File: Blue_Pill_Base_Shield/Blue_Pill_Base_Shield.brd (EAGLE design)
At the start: 54.2 x 36.7 mm, 15 parts, among them J1 4P-2.0, J2 4P-2.0, J3 4P-2.0, J4 4P-2.0, J5 4P-2.0, J6 4P-2.0, J7 4P-2.0, J8 4P-2.0

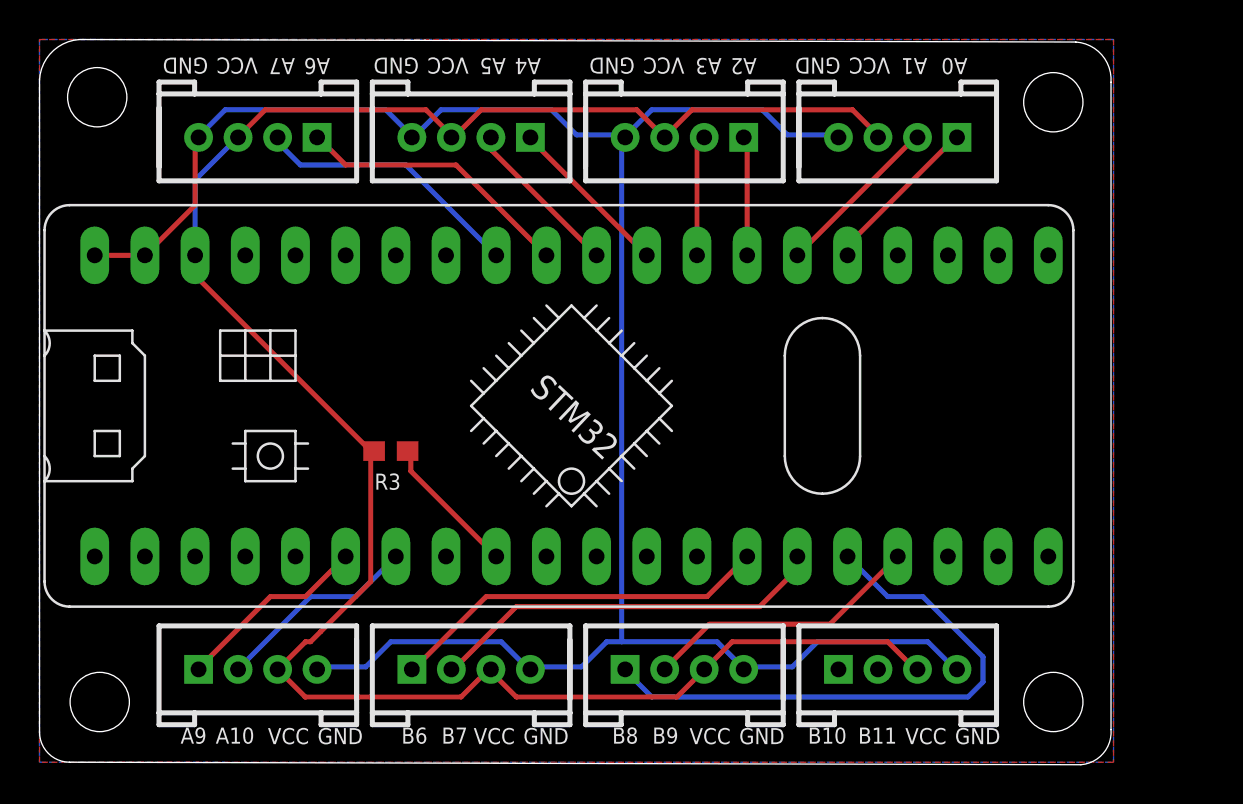
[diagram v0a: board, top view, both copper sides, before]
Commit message: Update Blue Pill Shield to add UART header
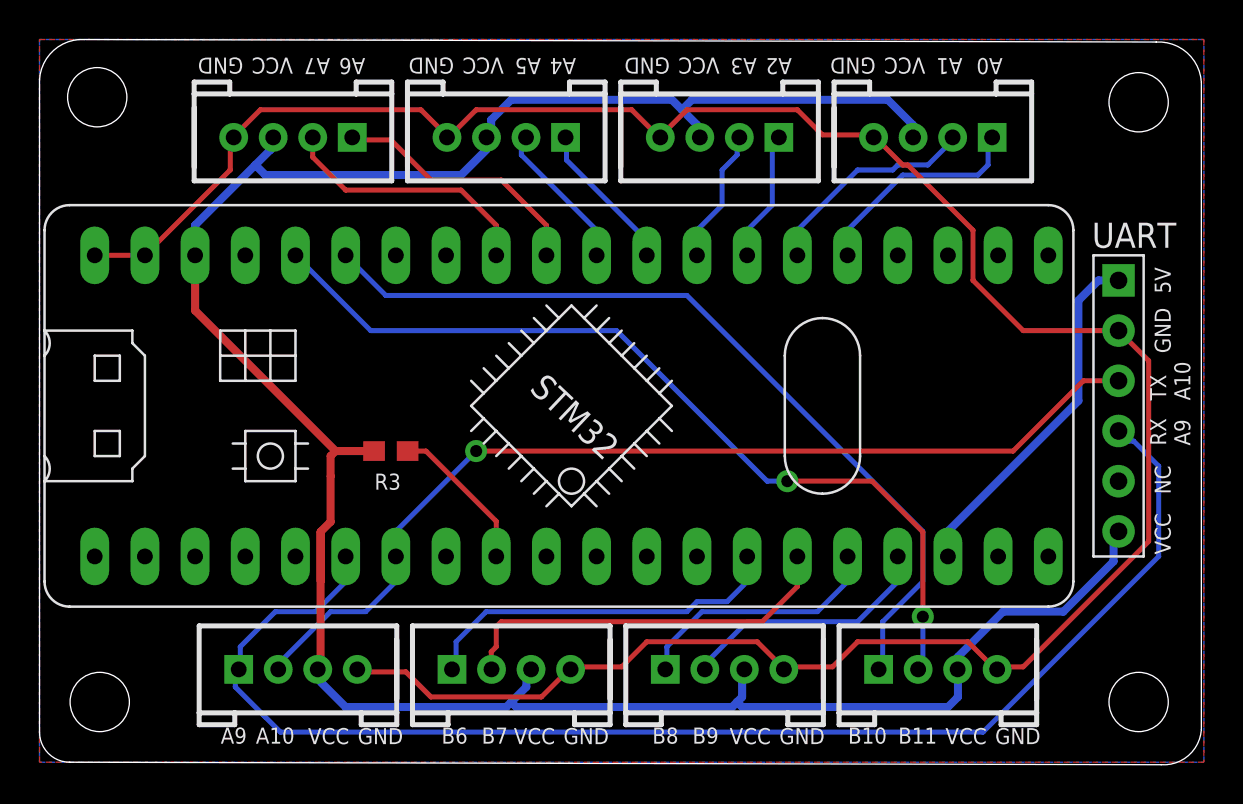
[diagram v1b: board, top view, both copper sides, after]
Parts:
- added UART: YELLOW-6P-2.54, Seeed-Connector:H6-2.54
- moved U$3 4.32 mm to (55.9, 32.9)
- moved U$4 4.32 mm to (55.9, 2.54)
- moved J1 2.03 mm to (13.3, 4.19)
- moved J2 2.03 mm to (24.1, 4.19)
- moved J3 2.03 mm to (34.9, 4.19)
- moved J4 2.03 mm to (45.7, 4.19)
- moved J6 1.78 mm to (23.9, 31.1)
- moved J5 1.78 mm to (13.1, 31.1)
- moved J7 1.78 mm to (34.7, 31.1)
- moved J8 1.78 mm to (45.5, 31.1)
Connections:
- removed net PB12: U$5.P$1
- new net 5V: U$5.P$18, UART.1
- new net NC: UART.5
- net DGND: now also UART.2
- net PA10: now also UART.3
- net PA9: now also UART.4
- net PB10: now also U$5.P$26
- net PB11: now also U$5.P$25
- net VCC: now also UART.6
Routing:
- net PA9: track 9.83 -> 69.0 mm
- net PB11: track 0.00 -> 44.6 mm, vias 0 -> 2
- net PB10: track 0.00 -> 42.9 mm
- net PA10: track 10.4 -> 50.2 mm, vias 0 -> 1
- net VCC: track 105.8 -> 129.9 mm
- net 5V: track 0.00 -> 18.1 mm
- net PB8: track 29.3 -> 12.9 mm
- net DGND: track 107.1 -> 121.8 mm
- net PA0: track 8.29 -> 11.3 mm
- net PA1: track 8.53 -> 11.2 mm
- net PB9: track 14.2 -> 13.0 mm
- net PA6: track 14.1 -> 13.2 mm
- net PA4: track 8.40 -> 7.66 mm
- net PA3: track 6.12 -> 6.85 mm
- net PA2: track 6.06 -> 6.62 mm
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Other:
- board size 54.2 x 36.7 mm -> 58.8 x 36.7 mm
- board text added: "5V"
- board text added: "NC"
- board text added: "RX A9"
- board text added: "TX A10"
